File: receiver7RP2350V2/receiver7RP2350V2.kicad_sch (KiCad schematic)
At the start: 71 parts, among them J1 BM04B-SRSS-TB, J10 S2B-PH-SM4-TB, J4 2pads, J6 MM60-52B1-E1-R650, J7 USB4105-GF-A, J8 S2B-PH-SM4-TB, U1 RP2350_60QFN, U2 USBLC6-2SC6, U3 AP7361C-33Y5-13, U4 MCP73871-2CCI_ML, U5 TPS610333DRLR, Y1 ABM8-272-T3

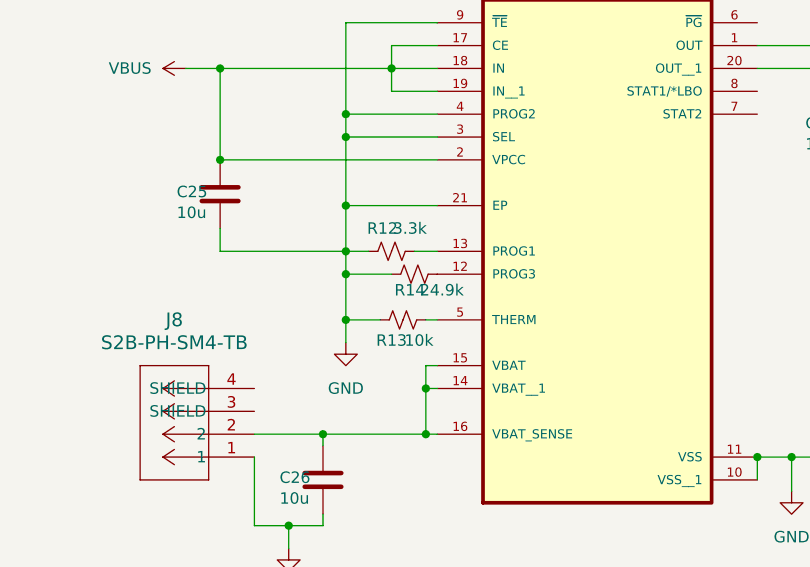
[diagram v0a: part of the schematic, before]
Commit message: add rp2350V2
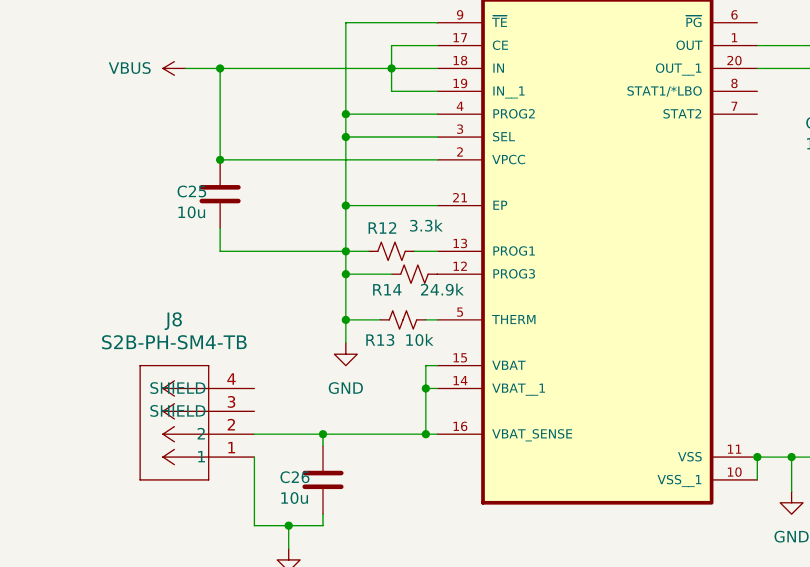
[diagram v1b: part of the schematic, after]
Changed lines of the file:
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@@
 		)
 		(property "Value" "3.3k"
-			(at 297.942 232.41 90)
+			(at 299.72 232.156 90)
 			(effects
 				(font
@@
 		(dnp no)
 		(property "Reference" "R14"
-			(at 297.942 239.268 90)
+			(at 295.402 239.268 90)
 			(effects
 				(font
@@
 		(dnp no)
 		(property "Reference" "R13"
-			(at 295.91 244.856 90)
+			(at 294.64 244.856 90)
 			(effects
 				(font

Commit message: add panelized files
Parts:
- removed C19, C29: 10u, Capacitor_SMD:C_0805_2012Metric, symbol Device:C
- removed H1, H2, H3, H4: MountingHole, receiverBoard:mountinghole3mm, symbol Mechanical:MountingHole
- removed L2: 1uH, EXLA1V0402_1RO_R:IND_EXLA-0402_EAT-L, symbol Device:L_Small
- removed R17: 750k, Resistor_SMD:R_0402_1005Metric, symbol Device:R_Small_US
- removed R18: 71.5k 1%, Resistor_SMD:R_0402_1005Metric, symbol Device:R_Small_US
- removed U3: AP7361C-33Y5-13, AP7361C_33Y5_13:SOT89-5_DIO-M_MODGND, symbol AP7361C_33Y5_13:AP7361C-33Y5-13
- removed U4: MCP73871-2CCI_ML, MCP73871_2CCI_ML:QFN50P400X400X100-21N, symbol MCP73871-2CCI_ML:MCP73871-2CCI_ML
- removed U5: TPS610333DRLR, TPS61033DRLR:DRL0008A-MFG_mod2, symbol TPS61033DRLR:TPS610333DRLR
- added C30: 10u, Capacitor_SMD:C_0805_2012Metric, symbol Device:C
- added D2: SMAJ6.0CA, Diode_SMD:D_SMA, symbol Diode:SMAJ6.0CA
- added H1: MountingHole, MountingHole:MountingHole_2.5mm, symbol receiverBoard:mountinghole4mm
- added J2, J3: NT4R1600, NT4R1600:JAE_Electronics-NT4R1600-MFG, symbol NT4R1600:NT4R1600
- added J5: USB4105-GF-A, USB4105_GF_A:GCT_USB4105-GF-A, symbol USB4105-GF-A:USB4105-GF-A
- added R19: 3.3k, Resistor_SMD:R_0402_1005Metric, symbol Device:R_Small_US
- added R20: 330k, Resistor_SMD:R_0402_1005Metric, symbol Device:R_Small_US
- added U4: MP2664GG-0000-Z, MP2664GG-0000-Z:QFN50P200X200X105-10N, symbol MP2664GG-0000-Z:MP2664GG-0000-Z
- added U5: NCP186AMX330TAG, NCP186AMX330TAG:PSON40P160X120X45-9N, symbol NCP186AMX330TAG:NCP186AMX330TAG
- C22, C23: value 10u -> 4.7u; footprint Capacitor_SMD:C_0805_2012Metric -> Capacitor_SMD:C_0402_1005Metric
- C25: value 10u -> 100n
- C26: footprint Capacitor_SMD:C_0402_1005Metric -> Capacitor_SMD:C_0805_2012Metric
- C27, C28: value 10u -> 4.7u
- H2: renamed from H5; footprint TF:MountingHole_4mm_t4 -> MountingHole:MountingHole_2.7mm_M2.5_Pad_Via
- H3: renamed from H6; footprint receiverBoard:mountinghole4mm -> MountingHole:MountingHole_2.7mm_M2.5_Pad_Via
- H4: renamed from H7; footprint receiverBoard:mountinghole4mm -> MountingHole:MountingHole_2.7mm_M2.5_Pad_Via
- H5: renamed from H8; footprint receiverBoard:mountinghole4mm -> MountingHole:MountingHole_2.7mm_M2.5_Pad_Via
- J1: footprint CONN4_BM04B-SRSS_JST -> BM04B_SRSS_TB:CONN4_BM04B-SRSS_JST
- R12: value 3.3k -> 10k
- R14: value 24.9k -> 3.3k
- R15, R16: value 3.3k -> 5.1k
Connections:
- net +5V is gone; now on net V_LOAD: C23.1
- net +3V3: now also C22.1, C28.1, R14.2, R19.2, U5.1 (OUT), U5.2 (OUT__1), U5.4 (FB/ADJ); no longer C22.2
- net GND: now also C22.2, C28.2, R16.2, C30.2, D2.1 (A1), J2.1, J3.1, J5.A1_B12 (GND), J5.B1_A12 (GND__1), J5.SH1 (SHELL_GND), J5.SH2 (SHELL_GND__1), J5.SH3 (SHELL_GND__2), J5.SH4 (SHELL_GND__3), U4.5 (GND), U5.3 (N/C), U5.5 (GND), U5.9 (EPAD); no longer C22.1, C28.1, R12.1, R14.1, R16.1
- net VBUS: now also C26.1, D2.2 (A2), J5.A4_B9 (VBUS), J5.B4_A9 (VBUS__1), U4.1 (IN); no longer C24.1, C25.1, J7.A4_B9 (VBUS), J7.B4_A9 (VBUS__1), U2.5
- net V_LOAD: now also J10.1, C30.1, U4.10 (SYS), U5.7 (IN), U5.8 (IN__1); no longer C27.1, C28.2
- net SDA0: now reaches U1.36 (GPIO24)
- net SDA0: now also R19.1, U4.7 (SDA)
- net SCL0: now reaches U1.37 (GPIO25)
- net SCL0: now also R14.1, U4.6 (SCL)
- net VDD: now reaches R12.2
- net VDD: now also C25.1, R20.2, U4.4 (VDD)
- net BAT_PWR: now reaches J8.2
- net BAT_PWR: now also C27.1, U4.8 (BATT), U4.9 (BATT); no longer C26.1
- net at R13.2: now also R12.1, U4.2 (NTC)
- net at R1.2, S1.4: no longer S1.3
- net at R15.2: now also J5.A5 (CC1); no longer J10.2
- net GPIO23 renamed INT_BAT
- net INT_BAT: now also R20.1, U4.3 (INT)
- new net: J5.B5 (CC2), R16.1
- new net VPHONE: C24.1, J7.A4_B9 (VBUS), J7.B4_A9 (VBUS__1), U2.5
- new net V_EN: J10.2, U5.6 (EN)
- no-connect marks 16 -> 15
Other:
- moved on the sheet: C1, C10, C11, C12, C13, C14, C15, C16, C17, C18, C2, C20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

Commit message: update to schematic
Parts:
- U1: value RP2350_60QFN -> RP2354_60QFN
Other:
- note removed: "12MHz Crystal"
- company: (none) -> North Carolina A&T State University
- title: (none) -> Handshake Receiver V2
- moved on the sheet: C1, C10, C11, C12, C13, C14, C15, C16, C17, C18, C2, C20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

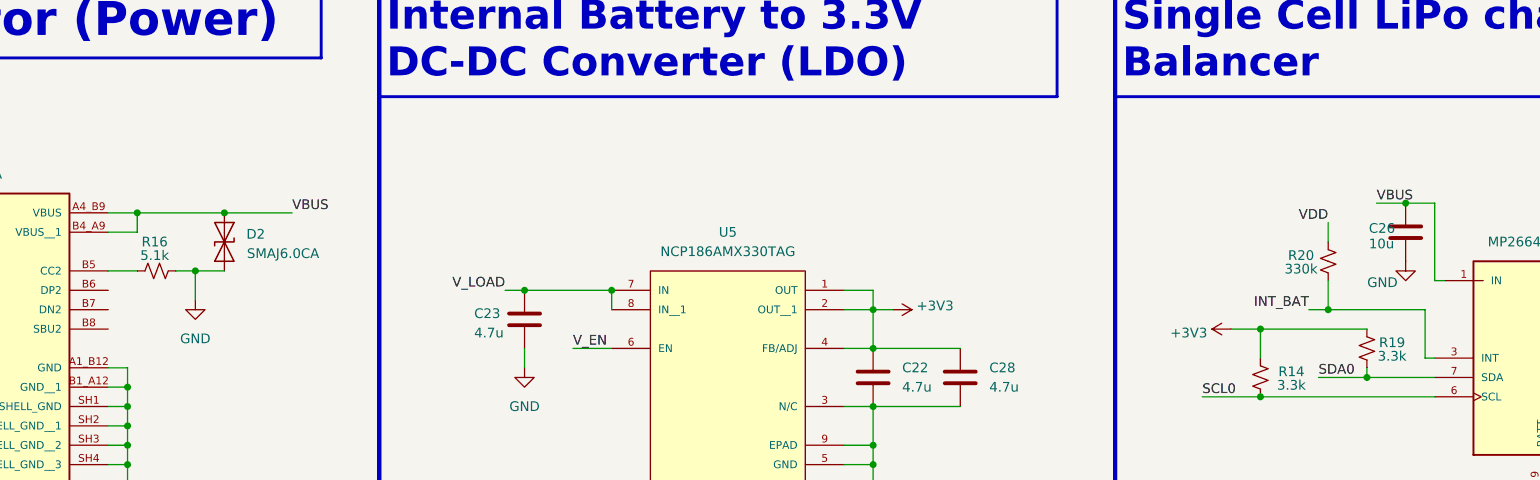
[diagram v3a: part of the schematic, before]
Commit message: updates to receiver layout
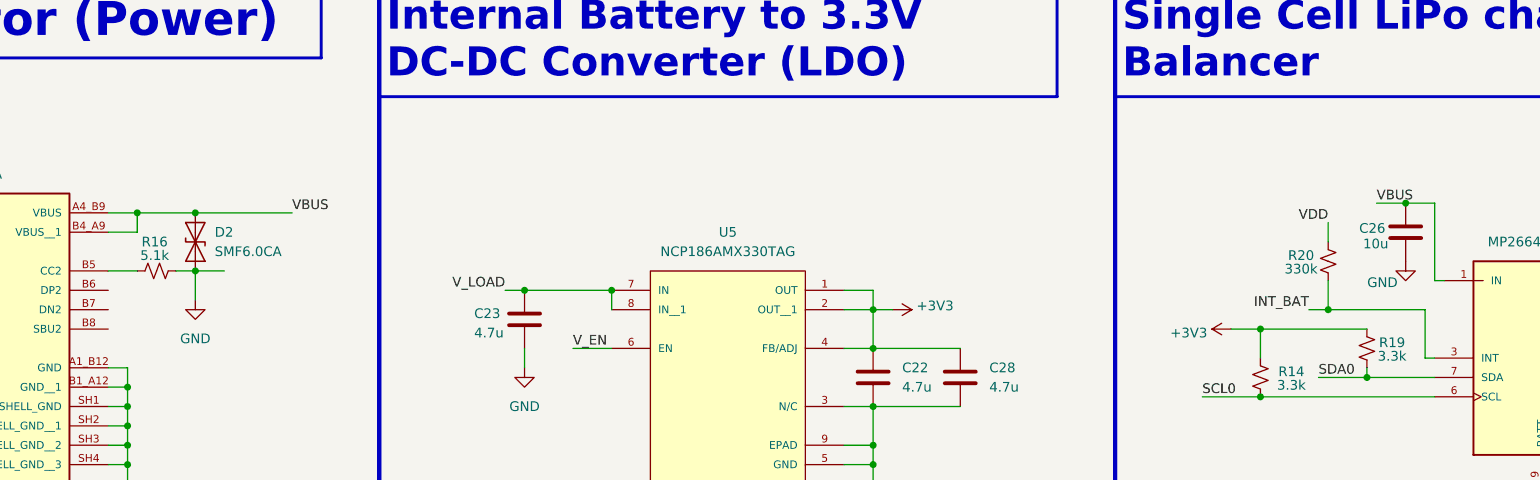
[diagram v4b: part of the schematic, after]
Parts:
- removed D2: SMAJ6.0CA, Diode_SMD:D_SMA, symbol Diode:SMAJ6.0CA
- added D2: SMF6.0CA, SMF26CA_custom:SMF26CA_Custom, symbol DM01:SMF6.0CA
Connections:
- net GND: now also D2.1 (A1)
- net VBUS: now also D2.2 (A2)
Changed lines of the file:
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@@
 	)
 	(junction
-		(at 93.98 151.13)
-		(diameter 0)
-		(color 0 0 0 0)
-	)
-	(junction
 		(at 300.99 66.04)
 		(diameter 0)
@@
 	)
 	(junction
+		(at 90.17 151.13)
+		(diameter 0)
+		(color 0 0 0 0)
+	)
+	(junction
 		(at 238.76 78.74)
 		(diameter 0)
@@
 	(wire
 		(pts
+			(xy 90.17 151.13) (xy 102.87 151.13)
+		)
+		(stroke
+			(width 0)
+			(type default)
+		)
+	)
+	(wire
+		(pts
 			(xy 290.83 35.56) (xy 281.94 35.56)
 		)
@@
 	(wire
 		(pts
-			(xy 93.98 151.13) (xy 102.87 151.13)
-		)
-		(stroke
-			(width 0)
-			(type default)
-		)
-	)
-	(wire
-		(pts
 			(xy 353.06 232.41) (xy 373.38 232.41)
 		)
@@
 	(wire
 		(pts
-			(xy 82.55 151.13) (xy 93.98 151.13)
+			(xy 82.55 151.13) (xy 90.17 151.13)
 		)
 		(stroke
@@
 		(dnp no)
 		(property "Reference" "C26"
-			(at 244.094 153.162 0)
+			(at 242.824 153.162 0)
 			(effects
 				(font
@@
 		)
 		(property "Value" "10u"
-			(at 244.094 155.194 0)
+			(at 243.332 155.194 0)
 			(effects
 				(font
@@
 	)
 	(symbol
-		(lib_id "Diode:SMAJ6.0CA")
-		(at 93.98 154.94 270)
-		(mirror x)
-		(unit 1)
-		(exclude_from_sim no)
-		(in_bom yes)
-		(on_board yes)
-		(dnp no)
-		(property "Reference" "D2"
-			(at 99.314 153.924 90)
-			(effects
-				(font
-					(size 1.27 1.27)
-				)
-				(justify right)
-			)
-		)
-		(property "Value" "SMAJ6.0CA"
-			(at 106.426 156.464 90)
-			(effects
-				(font
-					(size 1.27 1.27)
-				)
-				(justify right)
-			)
-		)
-		(property "Footprint" "Diode_SMD:D_SMA"
-			(at 88.9 154.94 0)
-			(effects
-				(font
-					(size 1.27 1.27)
-				)
-				(hide yes)
-			)
-		)
-		(property "Datasheet" "https://www.littelfuse.com/media?resourcetype=datasheets&itemid=75e32973-b177-4ee3-a0ff-cedaf1abdb93&filename=smaj-datasheet"
-			(at 93.98 154.94 0)
-			(effects
-				(font
-					(size 1.27 1.27)
-				)
-				(hide yes)
-			)
-		)
-		(property "Description" "400W bidirectional Transient Voltage Suppressor, 6.0Vr, SMA(DO-214AC)"
-			(at 93.98 154.94 0)
-			(effects
-				(font
-					(size 1.27 1.27)
-				)
-				(hide yes)
-			)
-		)
-		(pin "2"
-		)
-		(pin "1"
-		)
-		(instances
-			(project ""
-				(path "/621c97d5-9fcb-4bcf-8fc1-cbce142bada2"
-					(reference "D2")
-					(unit 1)
-				)
-			)
-		)
-	)
-	(symbol
 		(lib_id "Device:R_Small_US")
 		(at 487.68 64.77 90)
@@
 					(unit 1)
 				)
+			)
+		)
+	)
+	(symbol
+		(lib_id "DM01:SMF6.0CA")
+		(at 90.17 154.94 90)
+		(unit 1)
+		(exclude_from_sim no)
+		(in_bom yes)
+		(on_board yes)
+		(dnp no)
+		(fields_autoplaced yes)
+		(property "Reference" "D2"
+			(at 92.71 153.6699 90)
+			(effects
+				(font
+					(size 1.27 1.27)
+				)
+				(justify right)
+			)
+		)
+		(property "Value" "SMF6.0CA"
+			(at 92.71 156.2099 90)
+			(effects
+				(font
+					(size 1.27 1.27)
+				)
+				(justify right)
+			)
+		)
+		(property "Footprint" "SMF26CA_custom:SMF26CA_Custom"
+			(at 95.25 154.94 0)
+			(effects
+				(font
+					(size 1.27 1.27)
+				)
+				(hide yes)
+			)
+		)
+		(property "Datasheet" "https://www.littelfuse.com/assetdocs/tvs-diodes-smf-datasheet?assetguid=7EB8A5B6-BDD0-4561-8F19-0C3CC6F9B2AF"
+			(at 90.17 154.94 0)
+			(effects
+				(font
+					(size 1.27 1.27)
+				)
+				(hide yes)
+			)
+		)
+		(property "Description" "200W bidirectional Transient Voltage Suppressor, 6.0Vr, SMA(DO-214AC)"
+			(at 90.17 154.94 0)
+			(effects
+				(font
+					(size 1.27 1.27)
+				)
+				(hide yes)
+			)
+		)
+		(pin "2"
+		)
+		(pin "1"
+		)
+		(instances
+			(project ""
+				(path "/621c97d5-9fcb-4bcf-8fc1-cbce142bada2"
+					(reference "D2")
+					(unit 1)
+				)
